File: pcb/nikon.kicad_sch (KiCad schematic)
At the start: 91 parts, among them J1 USB_C_Receptacle_USB2.0, J2 AVR-ISP-6, J3 SJ2-35894A-SMT-TR, SW1 SW_Push, U1 ATmega32U4-AU, Y1 16MHz

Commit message: ...........
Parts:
- removed J1: USB_C_Receptacle_USB2.0, nikon:USB_C_GCT_USB4085, symbol Connector:USB_C_Receptacle_USB2.0
- removed J3: SJ2-35894A-SMT-TR, CUI_SJ2-35894A-SMT-TR, symbol nikon:SJ2-35894A-SMT-TR
- added D35, D36, D37, D38, D39, D40, D41, D42, D43, D44, D45, D46, D47, D48, D49, D50, D51, D52, D53, D54, D55, D56, D57, D58, D59, D60, D61, D62, D63, D64, D65, D66, D67, D68: 1N4148, Diode_SMD:D_SOD-123F, symbol Device:D_Small
- added J1: USB4105-GF-A, nikon:GCT_USB4105-GF-A, symbol nikon:USB4105-GF-A
- added J3: SJ2-35954A-SMT-TR, nikon:CUI_SJ2-35954A-SMT-TR, symbol nikon:SJ2-35954A-SMT-TR
- added MX35, MX36, MX37, MX38, MX43, MX48: MX-NoLED, nikon:SW_Kailh_Choc_V1_1.50u, symbol nikon:MX-NoLED
- added MX39, MX40, MX41, MX42, MX44, MX45, MX46, MX47, MX49, MX50, MX51, MX52, MX53, MX54, MX55, MX56, MX57, MX58, MX59, MX60, MX61, MX62, MX63, MX64, MX65, MX66, MX67, MX68: MX-NoLED, nikon:SW_Kailh_Choc_V1_1.00u, symbol nikon:MX-NoLED
- MX20: footprint nikon:SW_Kailh_Choc_V1_1.50u -> nikon:SW_Kailh_Choc_V1_1.00u
- R7, R8: renamed from R?; value R -> 4.7k; footprint (none) -> Resistor_SMD:R_0805_2012Metric_Pad1.20x1.40mm_HandSolder
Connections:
- net +5V: now also J3.4
- net D+: now also R3.2; no longer R3.1
- net D-: now also R2.2; no longer R2.1
- net GND: now also R4.2, J1.A1_B12 (GND), J1.B1_A12 (GND), J1.S1 (SHELL_GND), J1.S2 (SHELL_GND), J1.S3 (SHELL_GND), J1.S4 (SHELL_GND), J3.1; no longer R4.1
- net SCL: now also J3.2
- net SDA: now also J3.3
- net USB_D+: now also R3.1, J1.A6 (DP1), J1.B6 (DP2); no longer R3.2
- net USB_D-: now also R2.1, J1.A7 (DN1), J1.B7 (DN2); no longer R2.2
- net at F1.2: now also J1.A4_B9 (VBUS), J1.B4_A9 (VBUS)
- net at R5.2: now also J1.B5 (CC2)
- net Col1 renamed LCol1
- net LCol1: now also MX64.1 (COL), MX65.1 (COL), MX66.1 (COL), MX67.1 (COL), MX68.1 (COL)
- net Col2 renamed LCol2
- net LCol2: now also MX59.1 (COL), MX60.1 (COL), MX61.1 (COL), MX62.1 (COL), MX63.1 (COL)
- net Col3 renamed LCol3
- net LCol3: now also MX54.1 (COL), MX55.1 (COL), MX56.1 (COL), MX57.1 (COL), MX58.1 (COL)
- net Col4 renamed LCol4
- net LCol4: now also MX49.1 (COL), MX50.1 (COL), MX51.1 (COL), MX52.1 (COL), MX53.1 (COL)
- net Col5 renamed LCol5
- net LCol5: now also MX44.1 (COL), MX45.1 (COL), MX46.1 (COL), MX47.1 (COL), MX48.1 (COL)
- net Col6 renamed LCol6
- net LCol6: now also MX39.1 (COL), MX40.1 (COL), MX41.1 (COL), MX42.1 (COL), MX43.1 (COL)
- net Col7 renamed LCol7
- net LCol7: now also MX35.1 (COL), MX36.1 (COL), MX37.1 (COL), MX38.1 (COL)
- net Row1 renamed LRow1
- net Row2 renamed LRow2
- net Row3 renamed LRow3
- net Row4 renamed LRow4
- net Row5 renamed LRow5
- new net: J1.A5 (CC1), R4.1
- new net: D39.2 (A), MX39.2 (ROW)
- new net: D46.2 (A), MX46.2 (ROW)
- new net: D63.2 (A), MX63.2 (ROW)
- new net: D35.2 (A), MX35.2 (ROW)
- new net: D60.2 (A), MX60.2 (ROW)
- new net: D58.2 (A), MX58.2 (ROW)
- new net: D45.2 (A), MX45.2 (ROW)
- new net: D37.2 (A), MX37.2 (ROW)
- new net: D41.2 (A), MX41.2 (ROW)
- new net: D43.2 (A), MX43.2 (ROW)
- new net: D68.2 (A), MX68.2 (ROW)
- new net: D40.2 (A), MX40.2 (ROW)
- new net: D49.2 (A), MX49.2 (ROW)
- new net: D59.2 (A), MX59.2 (ROW)
- new net: D50.2 (A), MX50.2 (ROW)
- new net: D51.2 (A), MX51.2 (ROW)
- new net: D54.2 (A), MX54.2 (ROW)
- new net: D64.2 (A), MX64.2 (ROW)
- new net: D65.2 (A), MX65.2 (ROW)
- new net: D42.2 (A), MX42.2 (ROW)
- new net: D67.2 (A), MX67.2 (ROW)
- new net: D38.2 (A), MX38.2 (ROW)
- new net: D53.2 (A), MX53.2 (ROW)
- new net: D52.2 (A), MX52.2 (ROW)
- new net: D44.2 (A), MX44.2 (ROW)
- new net: D56.2 (A), MX56.2 (ROW)
- new net: D66.2 (A), MX66.2 (ROW)
- new net: D36.2 (A), MX36.2 (ROW)
- new net: D61.2 (A), MX61.2 (ROW)
- new net: D57.2 (A), MX57.2 (ROW)
- new net: D48.2 (A), MX48.2 (ROW)
- new net: D62.2 (A), MX62.2 (ROW)
- new net: D55.2 (A), MX55.2 (ROW)
- new net: D47.2 (A), MX47.2 (ROW)
- new net RRow1: D39.1 (K), D44.1 (K), D49.1 (K), D54.1 (K), D59.1 (K), D64.1 (K)
- new net RRow2: D35.1 (K), D40.1 (K), D45.1 (K), D50.1 (K), D55.1 (K), D60.1 (K), D65.1 (K)
- new net RRow3: D36.1 (K), D41.1 (K), D46.1 (K), D51.1 (K), D56.1 (K), D61.1 (K), D66.1 (K)
- new net RRow4: D37.1 (K), D42.1 (K), D47.1 (K), D52.1 (K), D57.1 (K), D62.1 (K), D67.1 (K)
- new net RRow5: D38.1 (K), D43.1 (K), D48.1 (K), D53.1 (K), D58.1 (K), D63.1 (K), D68.1 (K)
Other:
- note added: "Left Half Matrix"
- note removed: "Keyswitches"
- moved on the sheet: C1, C2, C3, C4, C5, C6, C7, C8, D1, D10, D11, D12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

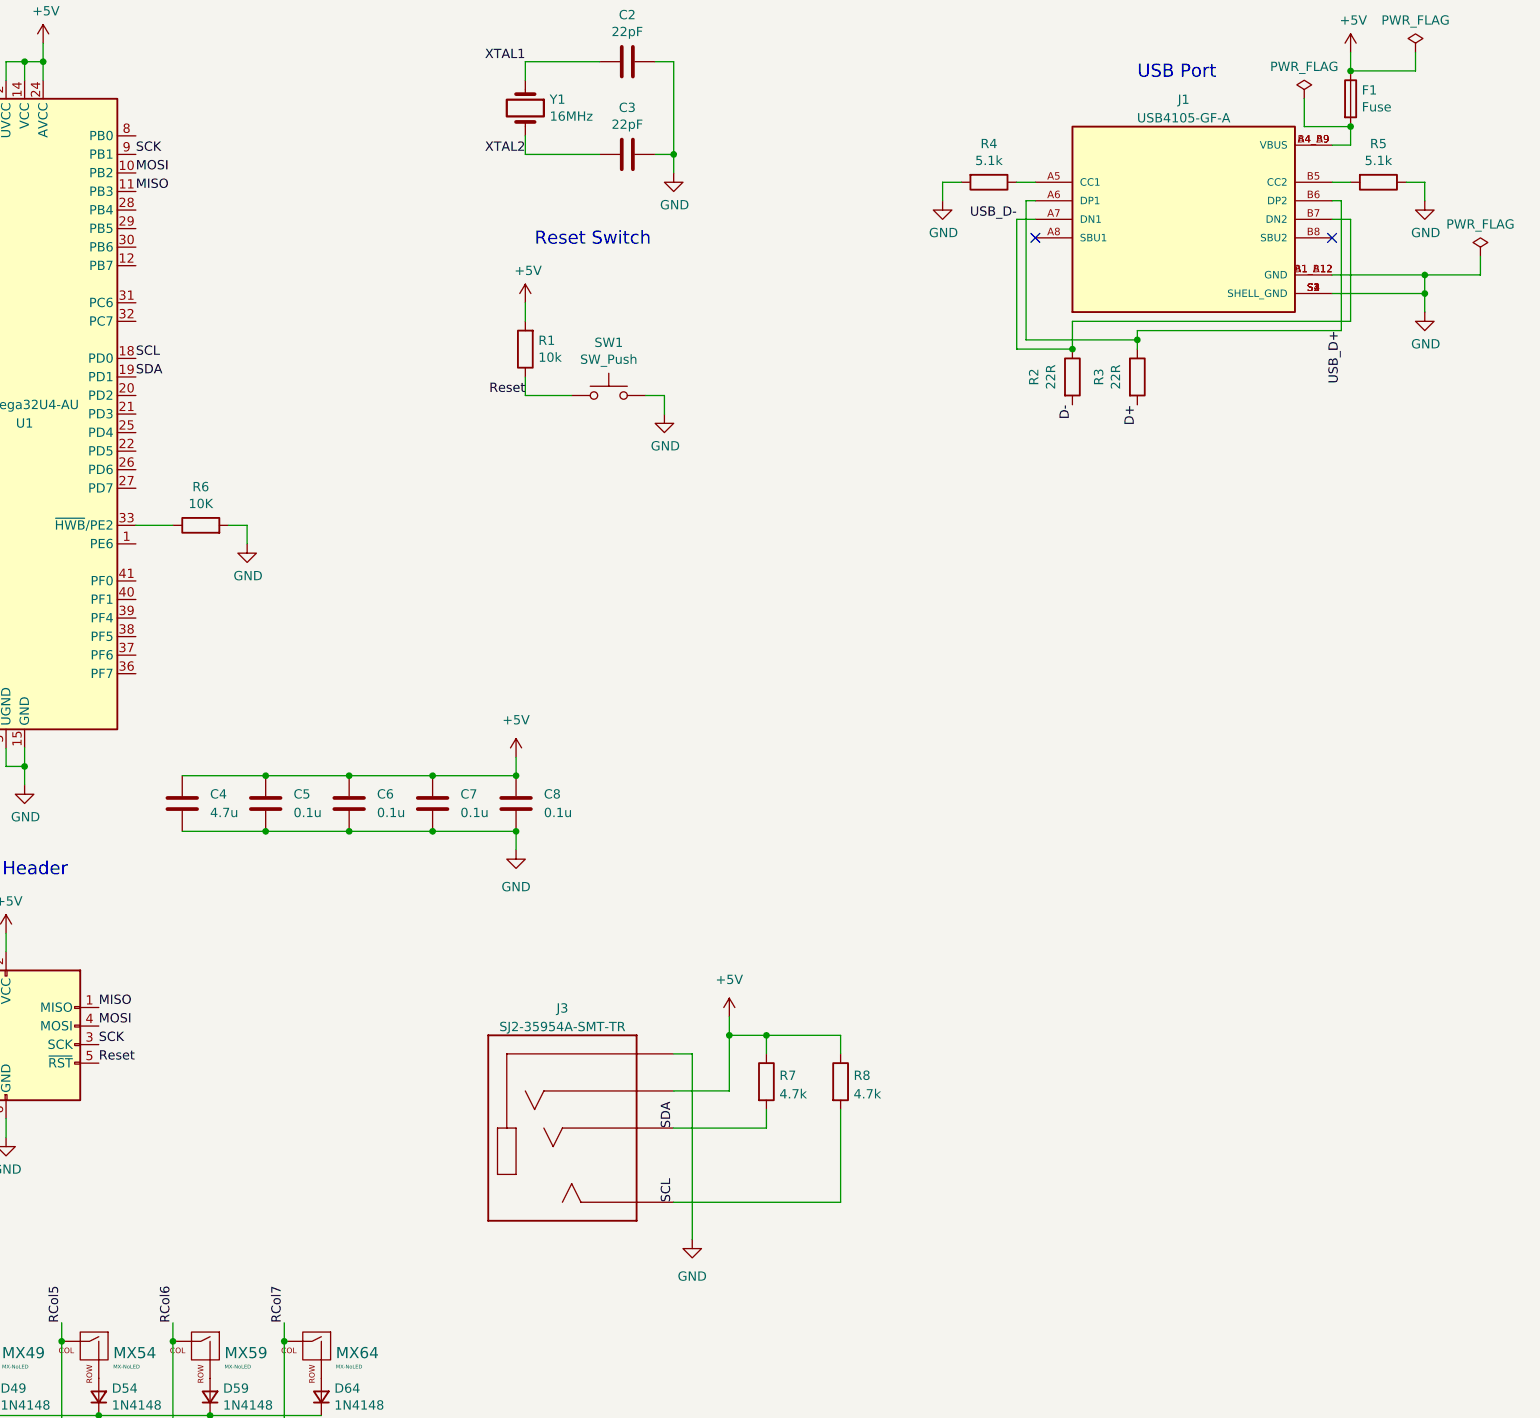
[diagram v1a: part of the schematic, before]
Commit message: remove right pcb
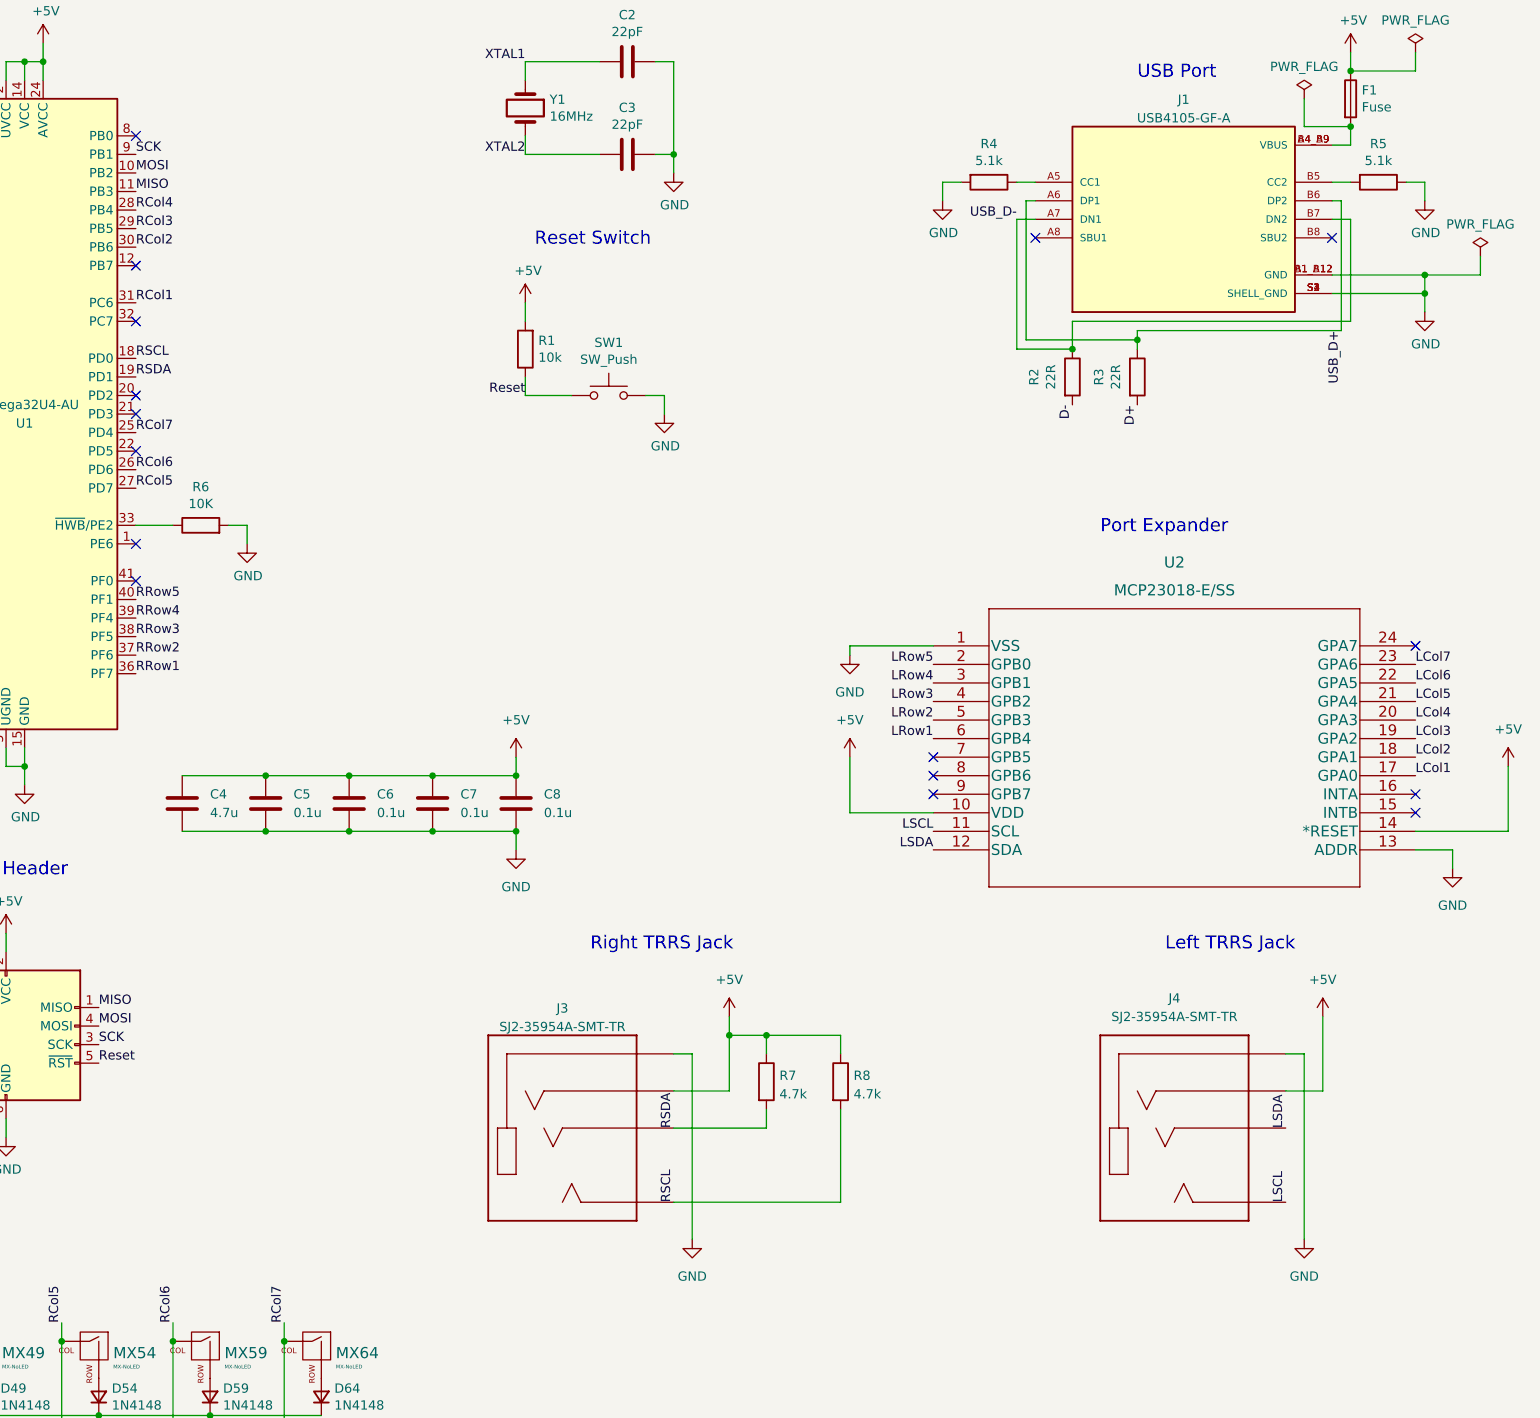
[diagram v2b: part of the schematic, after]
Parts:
- added J4: SJ2-35954A-SMT-TR, nikon:CUI_SJ2-35954A-SMT-TR, symbol nikon:SJ2-35954A-SMT-TR
- added U2: MCP23018-E/SS, nikon:MCP23018-E&slash_SS, symbol nikon:MCP23018-E{brace}slash}SS
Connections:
- net +5V: now also J4.4, U2.10 (VDD), U2.14 (*RESET)
- net GND: now also J4.1, U2.1 (VSS), U2.13 (ADDR)
- net LCol1: now also U1.25 (PD4), U2.17 (GPA0)
- net LCol2: now also U1.26 (PD6), U2.18 (GPA1)
- net LCol3: now also U1.27 (PD7), U2.19 (GPA2)
- net LCol4: now also U1.28 (PB4), U2.20 (GPA3)
- net LCol5: now also U1.29 (PB5), U2.21 (GPA4)
- net LCol6: now also U1.30 (PB6), U2.22 (GPA5)
- net LCol7: now also U1.31 (PC6), U2.23 (GPA6)
- net LRow1: now also U2.6 (GPB4)
- net LRow2: now also U2.5 (GPB3)
- net LRow3: now also U2.4 (GPB2)
- net LRow4: now also U2.3 (GPB1)
- net LRow5: now also U2.2 (GPB0)
- net RRow1: now also U1.36 (PF7)
- net RRow2: now also U1.37 (PF6)
- net RRow3: now also U1.38 (PF5)
- net RRow4: now also U1.39 (PF4)
- net RRow5: now also U1.40 (PF1)
- net SCL renamed RSCL
- net SDA renamed RSDA
- new net LSCL: J4.2, U2.11 (SCL)
- new net LSDA: J4.3, U2.12 (SDA)
- no-connect marks 3 -> 17
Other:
- note added: "Left TRRS Jack"
- note added: "Port Expander"
- note added: "Right TRRS Jack"

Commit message: 1.0
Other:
- note added: "Left Half"
- note added: "Overlapping Connections"
- note added: "Right Half"
- note added: "Right Half Matrix"
- title: (none) -> nikon
- moved on the sheet: C1, C2, C3, C4, C5, C6, C7, C8, D1, D10, D11, D12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

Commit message: esd
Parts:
- added C9: 0.1u, Capacitor_SMD:C_0805_2012Metric_Pad1.18x1.45mm_HandSolder, symbol Device:C
- added D?: PRTR5V0U2X, Package_TO_SOT_SMD:SOT-143, symbol Power_Protection:PRTR5V0U2X
- added U?: TPD2EUSB30, Package_TO_SOT_SMD:Texas_DRT-3, symbol Power_Protection:TPD2EUSB30
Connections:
- net +5V: now also C9.1
- net GND: now also C9.2
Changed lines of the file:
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@@
     (stroke (width 0) (type default) (color 0 0 0 0))
   )
+  (wire (pts (xy 304.8 134.62) (xy 316.23 134.62))
+    (stroke (width 0) (type default) (color 0 0 0 0))
+  )
   (wire (pts (xy 252.73 100.33) (xy 257.81 100.33))
     (stroke (width 0) (type default) (color 0 0 0 0))
@@
     (stroke (width 0) (type default) (color 0 0 0 0))
   )
+  (wire (pts (xy 304.8 142.24) (xy 316.23 142.24))
+    (stroke (width 0) (type default) (color 0 0 0 0))
+  )
   (wire (pts (xy 306.07 71.12) (xy 303.53 71.12))
     (stroke (width 0) (type default) (color 0 0 0 0))
@@
     (pin "1")
   )
+  (symbol (lib_id "Device:C") (at 316.23 138.43 0) (unit 1)
+    (in_bom yes) (on_board yes) (fields_autoplaced)
+    (property "Reference" "C9" (id 0) (at 319.151 137.5953 0)
+      (effects (font (size 1.27 1.27)) (justify left))
+    )
+    (property "Value" "0.1u" (id 1) (at 319.151 140.1322 0)
+      (effects (font (size 1.27 1.27)) (justify left))
+    )
+    (property "Footprint" "Capacitor_SMD:C_0805_2012Metric_Pad1.18x1.45mm_HandSolder" (id 2) (at 317.1952 142.24 0)
+      (effects (font (size 1.27 1.27)) hide)
+    )
+    (property "Datasheet" "~" (id 3) (at 316.23 138.43 0)
+      (effects (font (size 1.27 1.27)) hide)
+    )
+    (pin "1")
+    (pin "2")
+  )
   (symbol (lib_id "nikon:MX-NoLED") (at 298.45 180.34 0) (mirror y) (unit 1)
     (in_bom yes) (on_board yes)
@@
     (pin "2")
   )
+  (symbol (lib_id "Power_Protection:PRTR5V0U2X") (at 198.12 139.7 0) (unit 1)
+    (in_bom yes) (on_board yes) (fields_autoplaced)
+    (property "Reference" "D?" (id 0) (at 212.5988 136.9909 0))
+    (property "Value" "PRTR5V0U2X" (id 1) (at 212.5988 139.5278 0))
+    (property "Footprint" "Package_TO_SOT_SMD:SOT-143" (id 2) (at 199.644 139.7 0)
+      (effects (font (size 1.27 1.27)) hide)
+    )
+    (property "Datasheet" "https://assets.nexperia.com/documents/data-sheet/PRTR5V0U2X.pdf" (id 3) (at 199.644 139.7 0)
+      (effects (font (size 1.27 1.27)) hide)
+    )
+    (pin "1")
+    (pin "2")
+    (pin "3")
+    (pin "4")
+  )
   (symbol (lib_id "nikon:MX-NoLED") (at 374.65 180.34 0) (mirror y) (unit 1)
     (in_bom yes) (on_board yes)
@@
     (pin "1")
   )
+  (symbol (lib_id "Power_Protection:TPD2EUSB30") (at 196.85 111.76 0) (unit 1)
+    (in_bom yes) (on_board yes) (fields_autoplaced)
+    (property "Reference" "U?" (id 0) (at 196.85 102.9802 0))
+    (property "Value" "TPD2EUSB30" (id 1) (at 196.85 105.5171 0))
+    (property "Footprint" "Package_TO_SOT_SMD:Texas_DRT-3" (id 2) (at 177.8 119.38 0)
+      (effects (font (size 1.27 1.27)) hide)
+    )
+    (property "Datasheet" "http://www.ti.com/lit/ds/symlink/tpd2eusb30a.pdf" (id 3) (at 196.85 111.76 0)
+      (effects (font (size 1.27 1.27)) hide)
+    )
+    (pin "1")
+    (pin "2")
+    (pin "3")
+  )
   (symbol (lib_id "Device:D_Small") (at 360.68 212.09 90) (unit 1)
     (in_bom yes) (on_board yes)
@@
       (reference "C8") (unit 1) (value "0.1u") (footprint "Capacitor_SMD:C_0805_2012Metric_Pad1.18x1.45mm_HandSolder")
     )
+    (path "/17511276-5717-4498-a5c2-6e1bdd07dec3"
+      (reference "C9") (unit 1) (value "0.1u") (footprint "Capacitor_SMD:C_0805_2012Metric_Pad1.18x1.45mm_HandSolder")
+    )
     (path "/00000000-0000-0000-0000-000062147b6d"
       (reference "D1") (unit 1) (value "1N4148") (footprint "Diode_SMD:D_SOD-123F")
@@
       (reference "D68") (unit 1) (value "1N4148") (footprint "Diode_SMD:D_SOD-123F")
     )
+    (path "/6d5c63d8-bcb7-4b38-a00d-c6c48fa4b1a8"
+      (reference "D?") (unit 1) (value "PRTR5V0U2X") (footprint "Package_TO_SOT_SMD:SOT-143")
+    )
     (path "/00000000-0000-0000-0000-0000623fb7b7"
       (reference "F1") (unit 1) (value "Fuse") (footprint "Fuse:Fuse_0805_2012Metric_Pad1.15x1.40mm_HandSolder")
@@
       (reference "U2") (unit 1) (value "MCP23018-E{slash}SS") (footprint "nikon:MCP23018-E&slash_SS")
     )
+    (path "/b1f59d9a-2da8-4b52-bbe9-54dbef277cd8"
+      (reference "U?") (unit 1) (value "TPD2EUSB30") (footprint "Package_TO_SOT_SMD:Texas_DRT-3")
+    )
     (path "/00000000-0000-0000-0000-0000623b5e07"
